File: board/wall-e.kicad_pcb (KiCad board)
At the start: 2 copper layers, 88.2 x 64.4 mm, 65 parts, among them J1 Raspberry_Pi_2_3, J10 PCA9685, J11 VL53L0X, J12 VL53L0X, J13 VL53L0X, J14 MotorDrv2, J15 Motor2, J16 IMU, J17 INA219, J18 INA219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

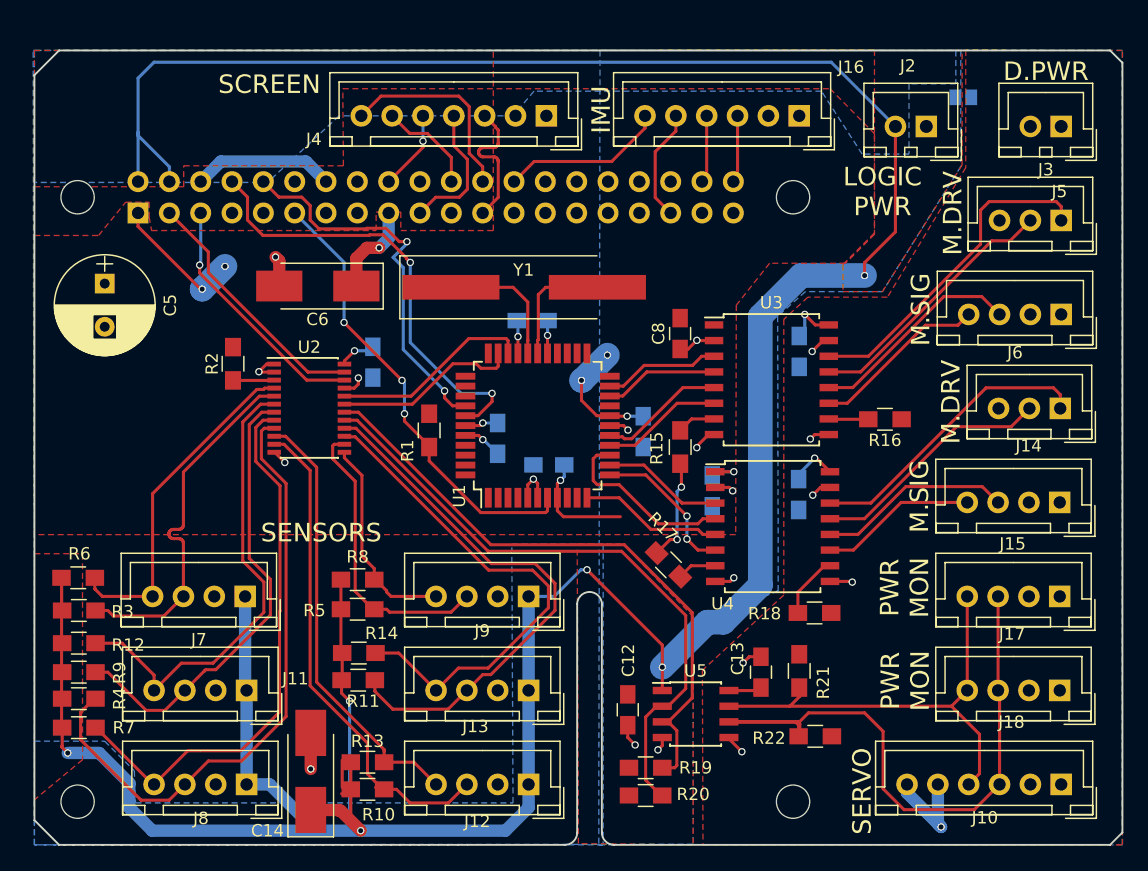
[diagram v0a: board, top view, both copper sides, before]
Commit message: Round corners.
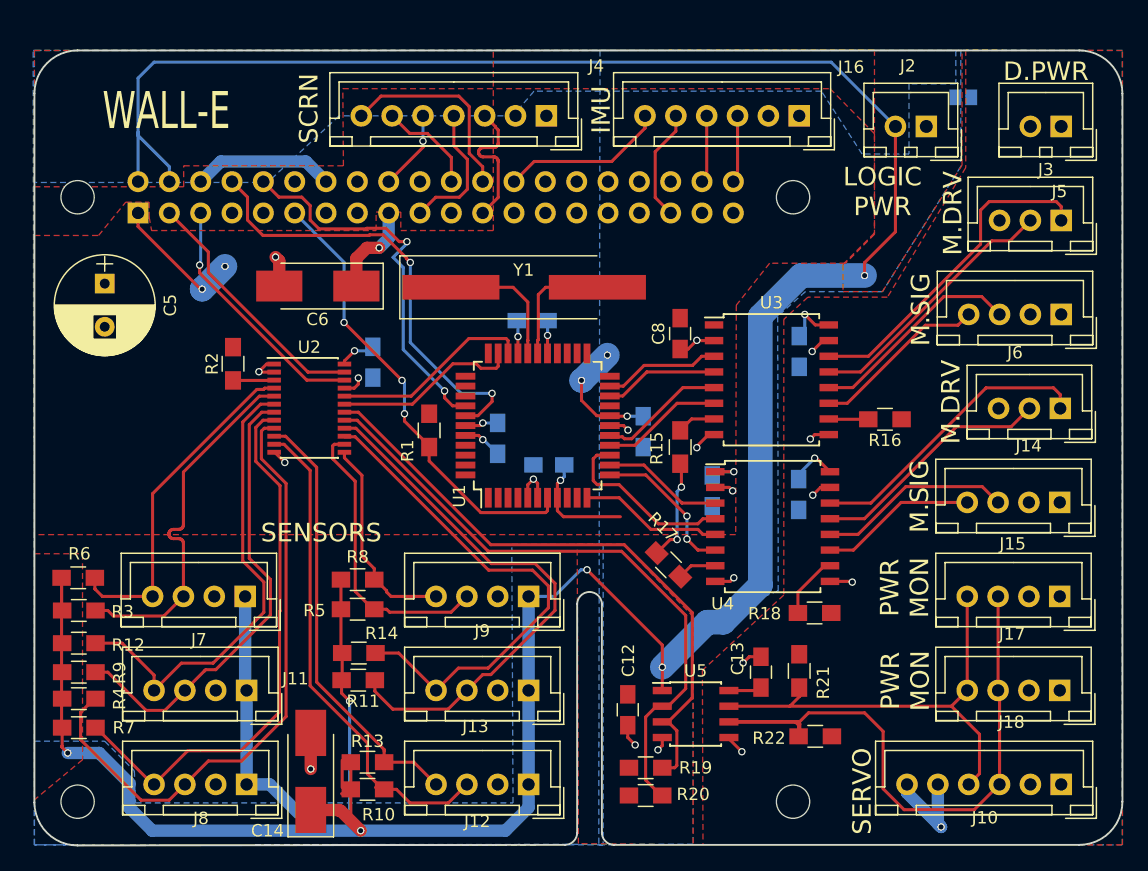
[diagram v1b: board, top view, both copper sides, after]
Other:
- outline, holes or cut-outs redrawn
- board text added: "SCRN"
- board text added: "WALL-E"
- board text removed: "SCREEN"
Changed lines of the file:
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@@
     (links 199)
     (no_connects 0)
-    (area 57.059999 14.759999 145.410001 79.310001)
+    (area 57.059999 14.759999 145.410001 79.360001)
     (thickness 1.6)
-    (drawings 67)
+    (drawings 68)
     (tracks 689)
     (zones 0)
@@
     (38 B.Mask user)
     (39 F.Mask user)
-    (40 Dwgs.User user)
+    (40 Dwgs.User user hide)
     (41 Cmts.User user hide)
     (42 Eco1.User user hide)
@@
     (trace_min 0.2)
     (segment_width 0.2)
-    (edge_width 0.15)
+    (edge_width 0.2)
     (via_size 0.6)
     (via_drill 0.4)
@@
     (descr "JST XH series connector, B07B-XH-A, top entry type, through hole")
     (tags "connector jst xh tht top vertical 2.50mm")
-    (fp_text reference J4 (at 18.85 -1.9 180) (layer F.SilkS)
+    (fp_text reference J4 (at -4.05 4.05 180) (layer F.SilkS)
       (effects (font (size 1 1) (thickness 0.15)))
     )
@@
     )
   )
+  (gr_text WALL-E (at 67.835 19.735) (layer F.SilkS)
+    (effects (font (size 3 2) (thickness 0.325)))
+  )
+  (gr_arc (start 141.835 18.335) (end 141.835 14.835) (angle 90) (layer Edge.Cuts) (width 0.15))
+  (gr_arc (start 141.835 75.735) (end 145.335 75.735) (angle 90) (layer Edge.Cuts) (width 0.15))
+  (gr_arc (start 60.635 75.785) (end 60.635 79.285) (angle 90) (layer Edge.Cuts) (width 0.15))
+  (gr_arc (start 60.635 18.335) (end 57.135 18.335) (angle 90) (layer Edge.Cuts) (width 0.15))
   (gr_text SENSORS (at 80.385 53.935 360) (layer F.SilkS)
     (effects (font (size 1.5 1.5) (thickness 0.3)))
@@
     (effects (font (size 1.5 1.5) (thickness 0.3)))
   )
-  (gr_text SCREEN (at 76.185 17.585) (layer F.SilkS)
+  (gr_text SCRN (at 79.385 19.535 90) (layer F.SilkS)
     (effects (font (size 1.5 1.5) (thickness 0.3)))
   )
@@
     (arrow2b (pts (xy 51.635 14.835) (xy 52.221421 15.961504)))
   )
-  (gr_line (start 100.135 79.235) (end 59.135 79.235) (layer Edge.Cuts) (width 0.15))
+  (gr_line (start 100.135 79.235) (end 60.635 79.285) (layer Edge.Cuts) (width 0.15))
   (gr_arc (start 100.135 78.235) (end 101.135 78.235) (angle 90) (layer Edge.Cuts) (width 0.15))
-  (gr_line (start 57.135 77.235) (end 59.135 79.235) (layer Edge.Cuts) (width 0.15))
-  (gr_line (start 59.135 14.835) (end 57.135 16.835) (layer Edge.Cuts) (width 0.15))
-  (gr_line (start 145.335 15.835) (end 144.335 14.835) (layer Edge.Cuts) (width 0.15))
-  (gr_line (start 145.335 78.235) (end 145.335 15.835) (layer Edge.Cuts) (width 0.15))
-  (gr_line (start 144.335 79.235) (end 145.335 78.235) (layer Edge.Cuts) (width 0.15))
+  (gr_line (start 145.335 75.735) (end 145.335 18.335) (layer Edge.Cuts) (width 0.15))
   (gr_line (start 126.135 59.735) (end 123.21 59.76) (layer Dwgs.User) (width 0.2))
   (gr_line (start 126.135 24.96) (end 126.135 59.735) (layer Dwgs.User) (width 0.2))
@@
   (gr_line (start 91.135 40.235) (end 91.135 55.235) (layer Dwgs.User) (width 0.2))
   (gr_line (start 76.135 40.235) (end 91.135 40.235) (layer Dwgs.User) (width 0.2))
-  (gr_line (start 59.135 14.835) (end 144.335 14.835) (layer Edge.Cuts) (width 0.15))
-  (gr_line (start 57.135 77.235) (end 57.135 16.835) (layer Edge.Cuts) (width 0.15))
-  (gr_line (start 144.335 79.235) (end 104.135 79.235) (layer Edge.Cuts) (width 0.15))
+  (gr_line (start 60.635 14.835) (end 141.835 14.835) (layer Edge.Cuts) (width 0.15))
+  (gr_line (start 57.135 75.785) (end 57.135 18.335) (layer Edge.Cuts) (width 0.15))
+  (gr_line (start 141.835 79.235) (end 104.135 79.235) (layer Edge.Cuts) (width 0.15))
   (gr_line (start 103.135 59.735) (end 103.135 78.235) (layer Edge.Cuts) (width 0.15))
   (gr_arc (start 102.135 59.735) (end 101.135 59.735) (angle 180) (layer Edge.Cuts) (width 0.15))

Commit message: ADd prototyping area.
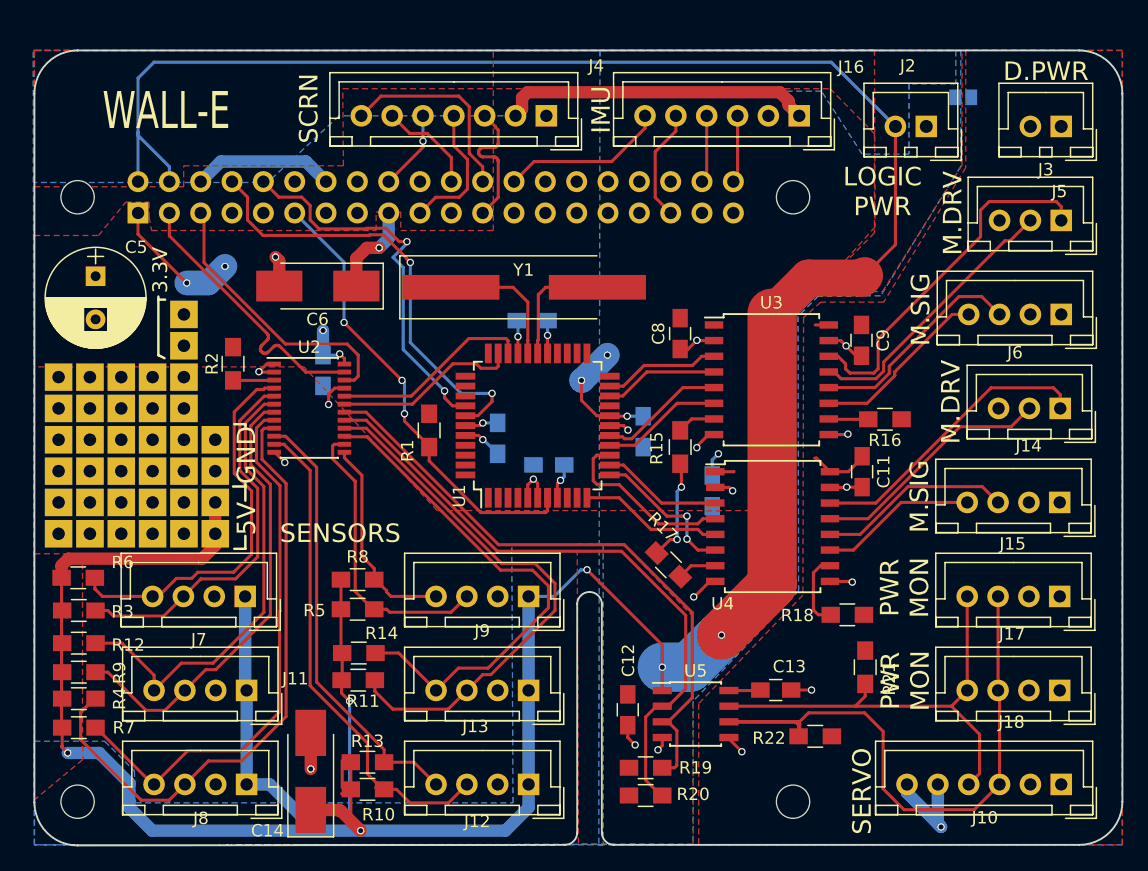
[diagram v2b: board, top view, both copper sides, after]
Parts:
- added ?: Sq_Pin, WallE:Sq_Pin, F.Cu at (71.8, 46.4)
- added ?: Sq_Pin, WallE:Sq_Pin, F.Cu at (61.6, 54.0)
- added ?: Sq_Pin, WallE:Sq_Pin, F.Cu at (59.1, 54.0)
- added ?: Sq_Pin, WallE:Sq_Pin, F.Cu at (69.3, 51.5)
- added ?: Sq_Pin, WallE:Sq_Pin, F.Cu at (66.7, 51.5)
- added ?: Sq_Pin, WallE:Sq_Pin, F.Cu at (64.2, 51.5)
- added ?: Sq_Pin, WallE:Sq_Pin, F.Cu at (61.6, 51.5)
- added ?: Sq_Pin, WallE:Sq_Pin, F.Cu at (59.1, 51.5)
- added ?: Sq_Pin, WallE:Sq_Pin, F.Cu at (69.3, 48.9)
- added ?: Sq_Pin, WallE:Sq_Pin, F.Cu at (66.7, 48.9)
- added ?: Sq_Pin, WallE:Sq_Pin, F.Cu at (64.2, 48.9)
- added ?: Sq_Pin, WallE:Sq_Pin, F.Cu at (71.8, 48.9)
- added ?: Sq_Pin, WallE:Sq_Pin, F.Cu at (61.6, 48.9)
- added ?: Sq_Pin, WallE:Sq_Pin, F.Cu at (59.1, 48.9)
- added ?: Sq_Pin, WallE:Sq_Pin, F.Cu at (69.3, 46.4)
- added ?: Sq_Pin, WallE:Sq_Pin, F.Cu at (66.7, 46.4)
- added ?: Sq_Pin, WallE:Sq_Pin, F.Cu at (64.2, 46.4)
- added ?: Sq_Pin, WallE:Sq_Pin, F.Cu at (61.6, 46.4)
- added ?: Sq_Pin, WallE:Sq_Pin, F.Cu at (59.1, 46.4)
- added ?: Sq_Pin, WallE:Sq_Pin, F.Cu at (69.3, 43.9)
- added ?: Sq_Pin, WallE:Sq_Pin, F.Cu at (66.7, 43.9)
- added ?: Sq_Pin, WallE:Sq_Pin, F.Cu at (64.2, 43.9)
- added ?: Sq_Pin, WallE:Sq_Pin, F.Cu at (71.8, 51.5)
- added ?: Sq_Pin, WallE:Sq_Pin, F.Cu at (61.6, 43.9)
- added ?: Sq_Pin, WallE:Sq_Pin, F.Cu at (59.1, 43.9)
- added ?: Sq_Pin, WallE:Sq_Pin, F.Cu at (69.3, 41.3)
- added ?: Sq_Pin, WallE:Sq_Pin, F.Cu at (66.7, 41.3)
- added ?: Sq_Pin, WallE:Sq_Pin, F.Cu at (64.2, 41.3)
- added ?: Sq_Pin, WallE:Sq_Pin, F.Cu at (61.6, 41.3)
- added ?: Sq_Pin, WallE:Sq_Pin, F.Cu at (71.8, 54.0)
- added ?: Sq_Pin, WallE:Sq_Pin, F.Cu at (59.1, 41.3)
- added ?: Sq_Pin, WallE:Sq_Pin, F.Cu at (69.3, 36.2)
- added ?: Sq_Pin, WallE:Sq_Pin, F.Cu at (69.3, 38.8)
- added ?: Sq_Pin, WallE:Sq_Pin, F.Cu at (69.3, 54.0)
- added ?: Sq_Pin, WallE:Sq_Pin, F.Cu at (66.7, 54.0)
- added ?: Sq_Pin, WallE:Sq_Pin, F.Cu at (64.2, 54.0)
- C11, C9: moved to F.Cu
- moved C11 5.47 mm to (124.2, 49.0)
- moved R21 5.36 mm to (124.5, 64.8)
- moved C9 5.13 mm to (124.2, 38.3)
- moved C7 4.09 mm to (80.5, 40.8)
- moved R18 2.66 mm to (123.0, 60.6)
- moved C13 1.88 mm to (117.2, 66.7), turned to 0 degrees
- moved C5 0.95 mm to (62.1, 33.1)
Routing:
- net +3V3: track 58.7 -> 79.5 mm, vias 13 -> 14
- net +5V: track 284.6 -> 303.7 mm
- net I2C_M0_SDA: track 27.6 -> 31.4 mm
- net GNDA: track 10.1 -> 12.9 mm
- net PI_I2C_SCLK: track 20.2 -> 22.7 mm, vias 1 -> 0
- net Net-(J5-Pad1): track 26.9 -> 29.4 mm
- net PI_I2C_SDA: track 20.5 -> 22.7 mm
- net +5VP: track 19.0 -> 16.8 mm, vias 3 -> 1
- net GND: track 44.0 -> 45.2 mm
- net Net-(R18-Pad2): track 5.17 -> 6.15 mm
- net I2C_M0_SCLK: track 29.7 -> 30.6 mm
- net Net-(J5-Pad2): track 21.4 -> 22.3 mm
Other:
- board text added: "3.3V"
- board text added: "5V"
- board text added: "GND"

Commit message: Tweaks.
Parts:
- moved R18 0.82 mm to (122.4, 61.1)
- moved R21 0.75 mm to (123.7, 64.9)
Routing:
- net PI_RX: track 31.2 -> 29.0 mm
- net Net-(R18-Pad2): track 6.15 -> 7.18 mm
- net I2C_M2_SCLK: track 50.7 -> 51.5 mm
- net +5V: vias 6 -> 7

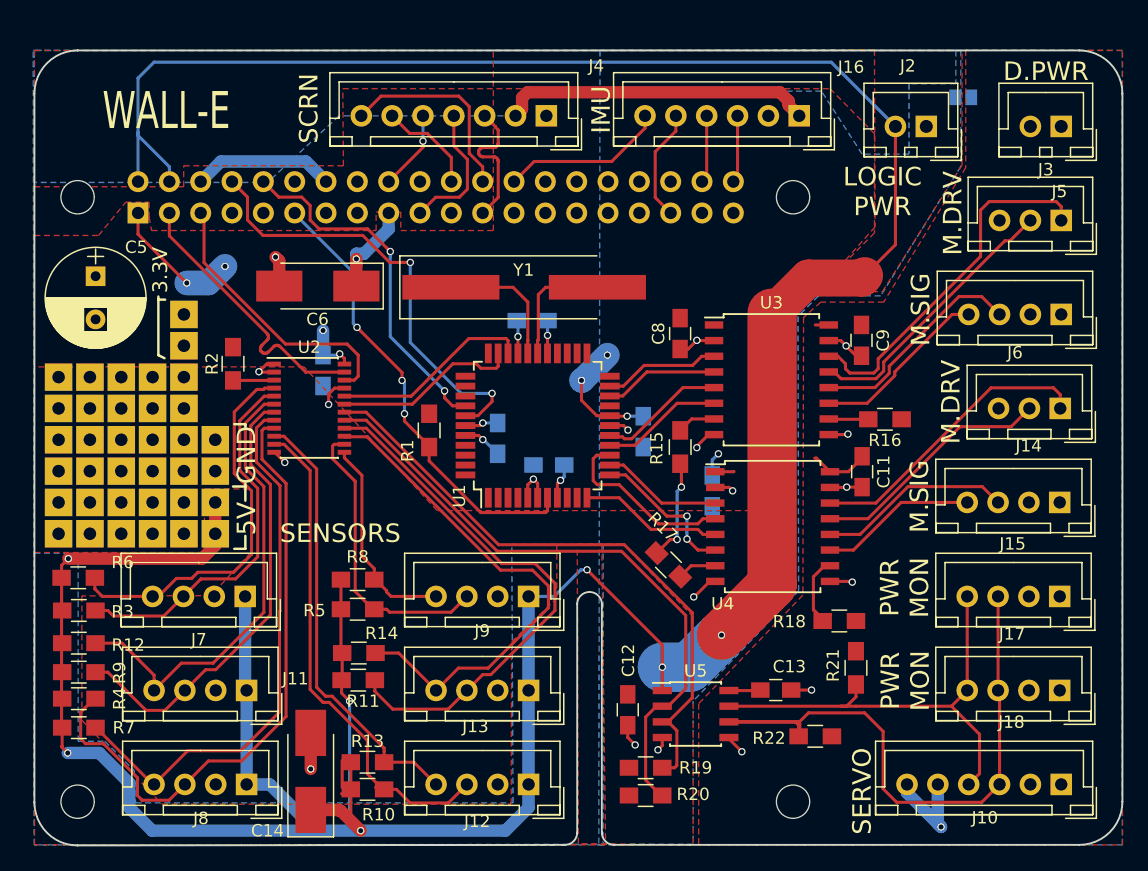
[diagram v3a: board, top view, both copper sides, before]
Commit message: Move power monitors onto logic power.
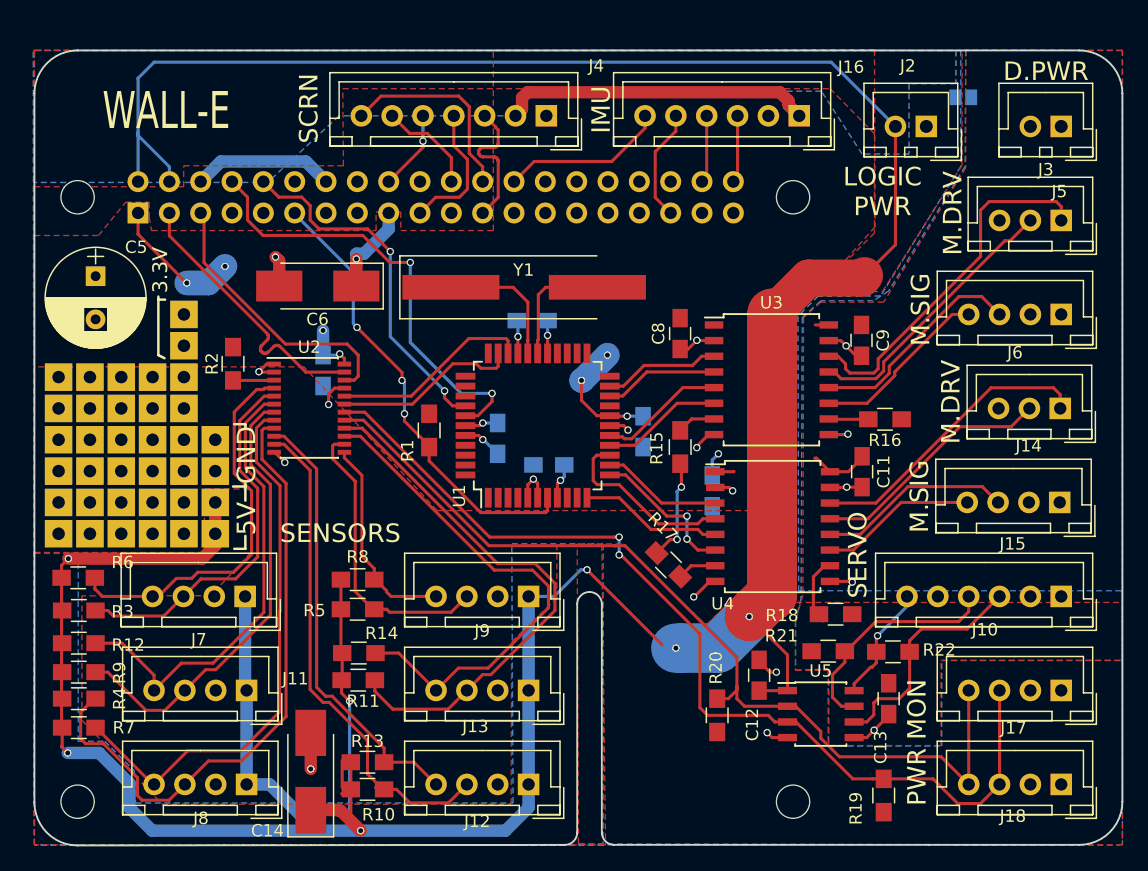
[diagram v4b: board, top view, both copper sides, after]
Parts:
- moved R19 19.4 mm to (126.0, 75.2), turned to 90 degrees
- moved J10 15.2 mm to (140.4, 59.1)
- moved C12 11.0 mm to (115.9, 65.5), turned to 90 degrees
- moved U5 10.2 mm to (120.9, 68.6)
- moved R22 9.31 mm to (126.7, 63.6), turned to 0 degrees
- moved C13 9.18 mm to (126.4, 67.4), turned to 270 degrees
- moved R20 8.71 mm to (112.5, 68.7), turned to 90 degrees
- moved J17 7.62 mm to (140.4, 66.7)
- moved J18 7.62 mm to (140.4, 74.3)
- moved R21 2.62 mm to (121.5, 63.5), turned to 0 degrees
- moved R18 0.63 mm to (122.1, 60.5)
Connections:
- J17 pad 1: +5VP -> +5V
- J17 pad 2: GNDA -> GND
- J17 pad 3: I2C_ISO_SCL -> I2C_M6_SCLK
- J17 pad 4: I2C_ISO_SDA -> I2C_M6_SDA
- J18 pad 1: +5VP -> +5V
- J18 pad 2: GNDA -> GND
- J18 pad 3: I2C_ISO_SCL -> I2C_M6_SCLK
- J18 pad 4: I2C_ISO_SDA -> I2C_M6_SDA
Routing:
- net I2C_ISO_SCL: track 53.2 -> 18.8 mm
- net I2C_M6_SCLK: track 50.2 -> 78.9 mm, vias 0 -> 2
- net +5V: track 303.7 -> 331.3 mm
- net I2C_M6_SDA: track 51.3 -> 74.9 mm
- net I2C_ISO_SDA: track 37.6 -> 18.8 mm
- net +5VP: track 16.8 -> 15.5 mm
- net Net-(R18-Pad2): track 7.18 -> 6.18 mm
- net GND: track 45.2 -> 45.9 mm
- net GNDA: track 12.9 -> 13.3 mm, vias 6 -> 5

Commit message: More proto area.
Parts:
- added ?: Sq_Pin, WallE:Sq_Pin, F.Cu at (112.4, 74.3)
- added ?: Sq_Pin, WallE:Sq_Pin, F.Cu at (104.8, 71.8)
- added ?: Sq_Pin, WallE:Sq_Pin, F.Cu at (104.8, 74.3)
- added ?: Sq_Pin, WallE:Sq_Pin, F.Cu at (107.4, 74.3)
- added ?: Sq_Pin, WallE:Sq_Pin, F.Cu at (107.4, 76.9)
- added ?: Sq_Pin, WallE:Sq_Pin, F.Cu at (104.8, 76.9)
- added ?: Sq_Pin, WallE:Sq_Pin, F.Cu at (112.4, 76.9)
- added ?: Sq_Pin, WallE:Sq_Pin, F.Cu at (104.8, 66.7)
- added ?: Sq_Pin, WallE:Sq_Pin, F.Cu at (107.4, 66.7)
- added ?: Sq_Pin, WallE:Sq_Pin, F.Cu at (109.9, 74.3)
- added ?: Sq_Pin, WallE:Sq_Pin, F.Cu at (109.9, 76.9)
- added ?: Sq_Pin, WallE:Sq_Pin, F.Cu at (104.8, 69.3)
- added ?: Sq_Pin, WallE:Sq_Pin, F.Cu at (107.4, 69.3)
- added ?: Sq_Pin, WallE:Sq_Pin, F.Cu at (107.4, 71.8)
- moved R20 0.95 mm to (113.4, 68.7)
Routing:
- net I2C_M6_SDA: track 74.9 -> 73.1 mm
